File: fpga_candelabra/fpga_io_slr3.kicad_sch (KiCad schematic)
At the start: 1 part, among them U1 XCVU13P-B2104

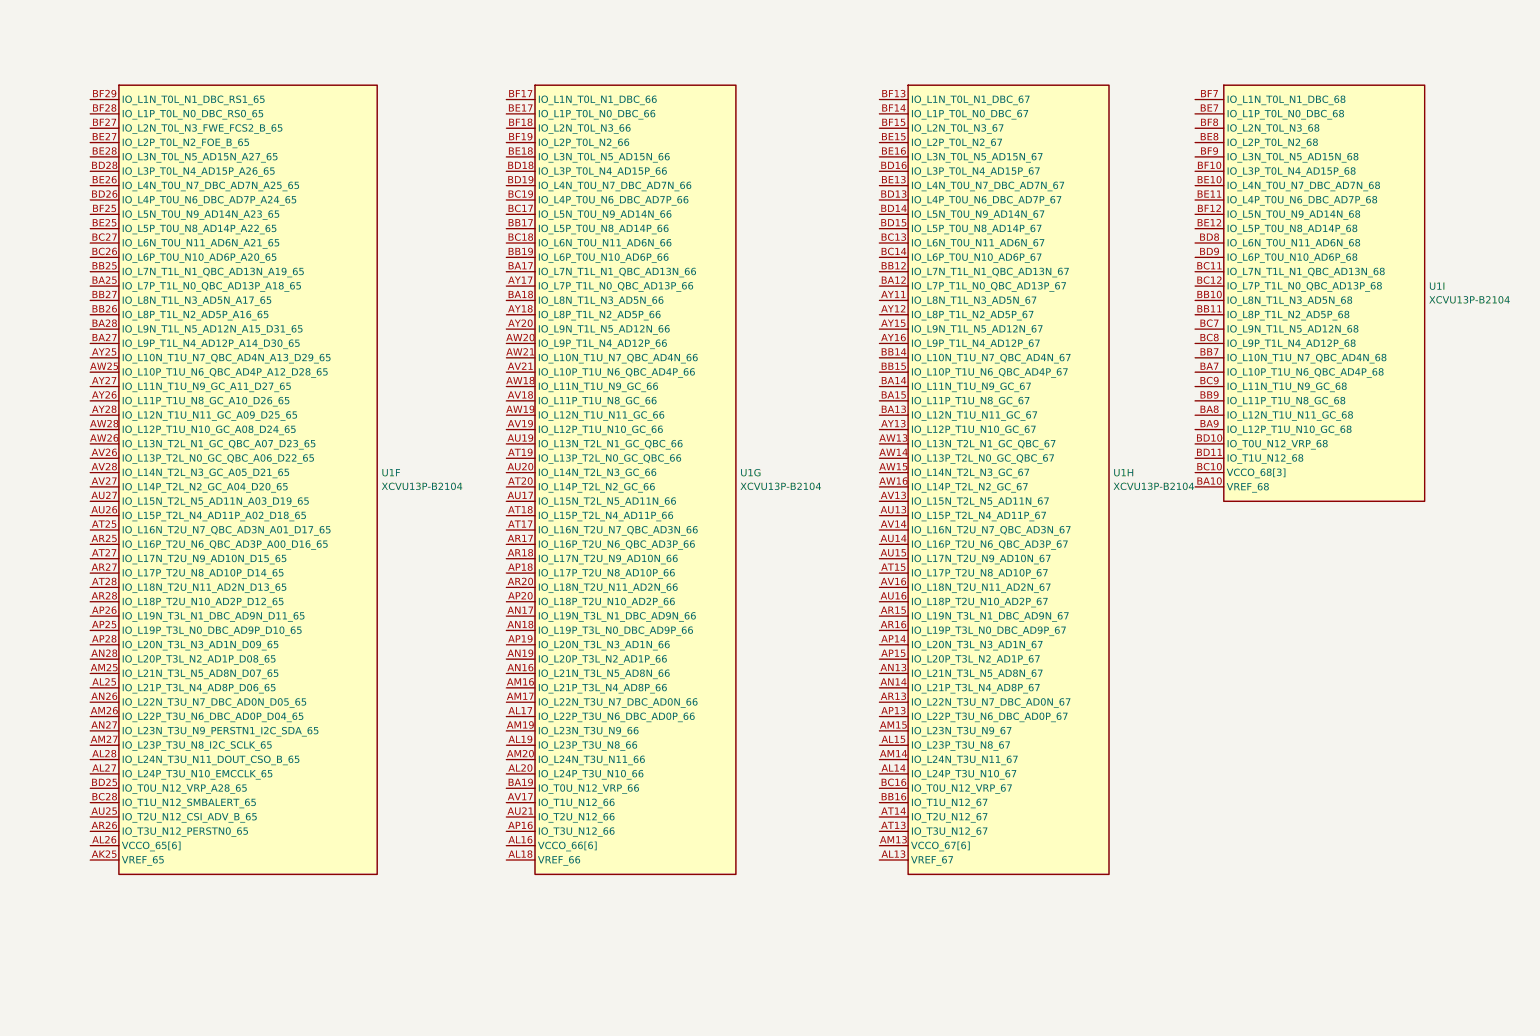
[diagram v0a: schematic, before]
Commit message: fpga_candelabra: reorganize fpga io and mgt by SLR
- Rename sch sheets
- Add prelimary DDR and PCIE Bank/Quad allocation

Signed-off-by: Yichuan Gao <gaoyichuan000@gmail.com>
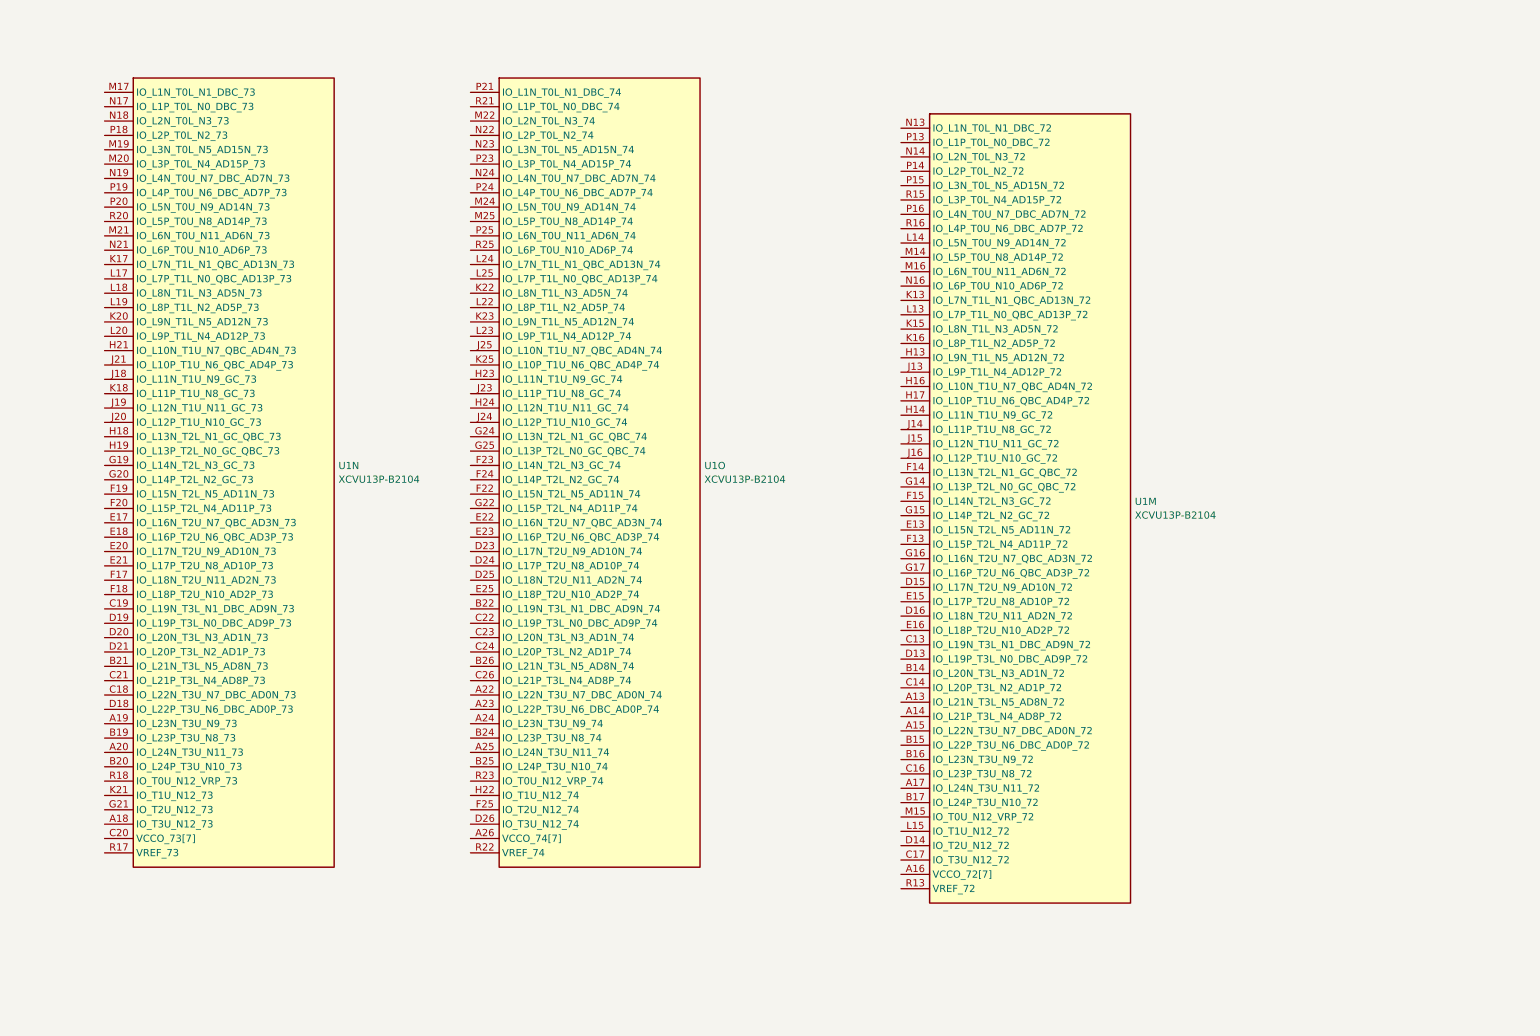
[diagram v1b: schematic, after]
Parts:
- removed U1: XCVU13P-B2104, CHIPSAlliance_Package_BGA:Xilinx_FHGB2104_VU13P_PkgLength, symbol CHIPSAlliance_FPGA_Xilinx_Virtex_UltraScale_Plus:XCVU13P-B2104
- added U1: XCVU13P-B2104, CHIPSAlliance_Package_BGA:Xilinx_FHGB2104_VU13P_PkgLength, symbol CHIPSAlliance_FPGA_Xilinx_Virtex_UltraScale_Plus:XCVU13P-B2104
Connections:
- new net: U1.A26 (VCCO_74[7]), U1.B23 (VCCO_74[7]), U1.E24 (VCCO_74[7]), U1.H25 (VCCO_74[7]), U1.J22 (VCCO_74[7]), U1.M23 (VCCO_74[7]), U1.R24 (VCCO_74[7])
- new net: U1.A16 (VCCO_72[7]), U1.B13 (VCCO_72[7]), U1.E14 (VCCO_72[7]), U1.H15 (VCCO_72[7]), U1.L16 (VCCO_72[7]), U1.M13 (VCCO_72[7]), U1.R14 (VCCO_72[7])
- new net: U1.C20 (VCCO_73[7]), U1.D17 (VCCO_73[7]), U1.F21 (VCCO_73[7]), U1.G18 (VCCO_73[7]), U1.K19 (VCCO_73[7]), U1.N20 (VCCO_73[7]), U1.P17 (VCCO_73[7])

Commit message: fpga_candelabra: use bus alias to connect ddr4
Signed-off-by: Yichuan Gao <gaoyichuan000@gmail.com>
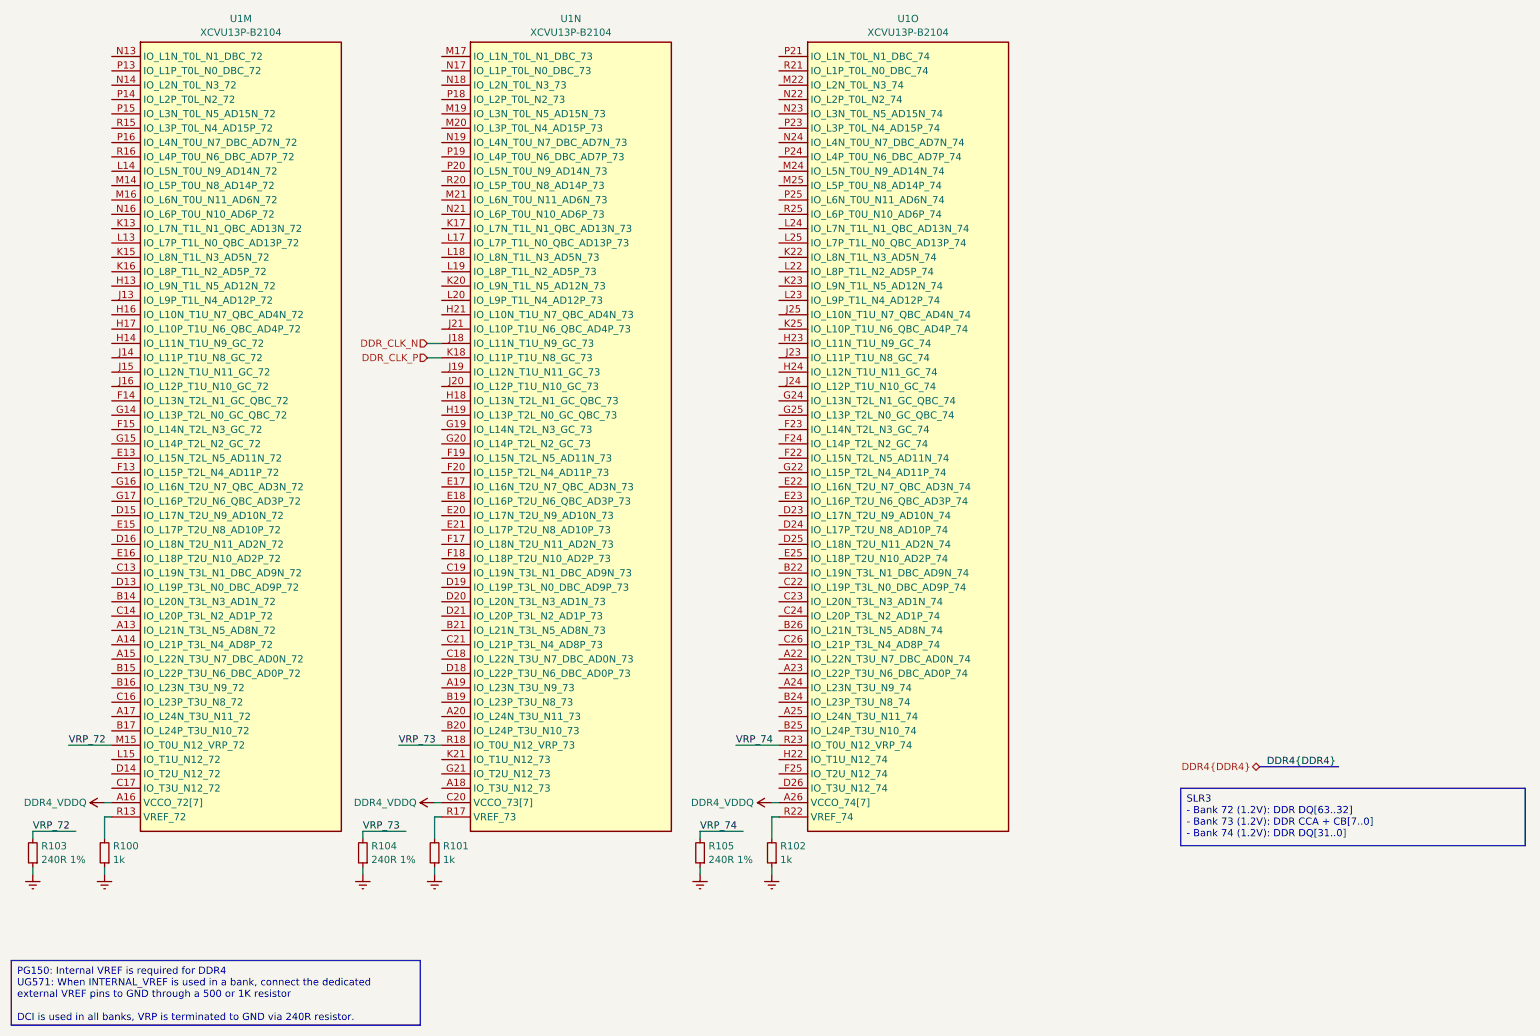
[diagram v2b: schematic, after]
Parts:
- added R100, R101, R102: 1k, Resistor_SMD:R_0402_1005Metric, symbol Device:R_Small
- added R103, R104, R105: 240R 1%, Resistor_SMD:R_0402_1005Metric, symbol Device:R_Small
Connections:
- net DDR4_VDDQ: now reaches U1.A26 (VCCO_74[7]), U1.B23 (VCCO_74[7]), U1.E24 (VCCO_74[7]), U1.H25 (VCCO_74[7]), U1.J22 (VCCO_74[7]), U1.M23 (VCCO_74[7]), U1.R24 (VCCO_74[7])
- net DDR4_VDDQ: now also U1.A16 (VCCO_72[7]), U1.B13 (VCCO_72[7]), U1.C20 (VCCO_73[7]), U1.D17 (VCCO_73[7]), U1.E14 (VCCO_72[7]), U1.F21 (VCCO_73[7]), U1.G18 (VCCO_73[7]), U1.H15 (VCCO_72[7]), U1.K19 (VCCO_73[7]), U1.L16 (VCCO_72[7]), U1.M13 (VCCO_72[7]), U1.N20 (VCCO_73[7]), U1.P17 (VCCO_73[7]), U1.R14 (VCCO_72[7])
- net at U1.R22 (VREF_74): now also R102.2
- net VRP_74: now reaches U1.R23 (IO_T0U_N12_VRP_74)
- net VRP_74: now also R105.2
- net VRP_72: now reaches U1.M15 (IO_T0U_N12_VRP_72)
- net VRP_72: now also R103.2
- net at U1.R13 (VREF_72): now also R100.2
- net DDR_CLK_N: now reaches U1.J18 (IO_L11N_T1U_N9_GC_73)
- net DDR_CLK_P: now reaches U1.K18 (IO_L11P_T1U_N8_GC_73)
- net at U1.R17 (VREF_73): now also R101.2
- net VRP_73: now reaches U1.R18 (IO_T0U_N12_VRP_73)
- net VRP_73: now also R104.2
- new net Earth: R100.1, R101.1, R102.1, R103.1, R104.1, R105.1
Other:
- moved on the sheet: U1M, U1N, U1O

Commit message: fpga_candelabra: fix minor issues in ddr sch
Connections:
- net DDR_CLK_N renamed DDR_CLK-
- net DDR_CLK_P renamed DDR_CLK+
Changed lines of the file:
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@@
 		)
 	)
-	(hierarchical_label "DDR_CLK_P"
+	(hierarchical_label "DDR_CLK+"
 		(shape input)
 		(at 88.9 77.47 180)
@@
 		)
 	)
-	(hierarchical_label "DDR_CLK_N"
+	(hierarchical_label "DDR_CLK-"
 		(shape input)
 		(at 88.9 74.93 180)

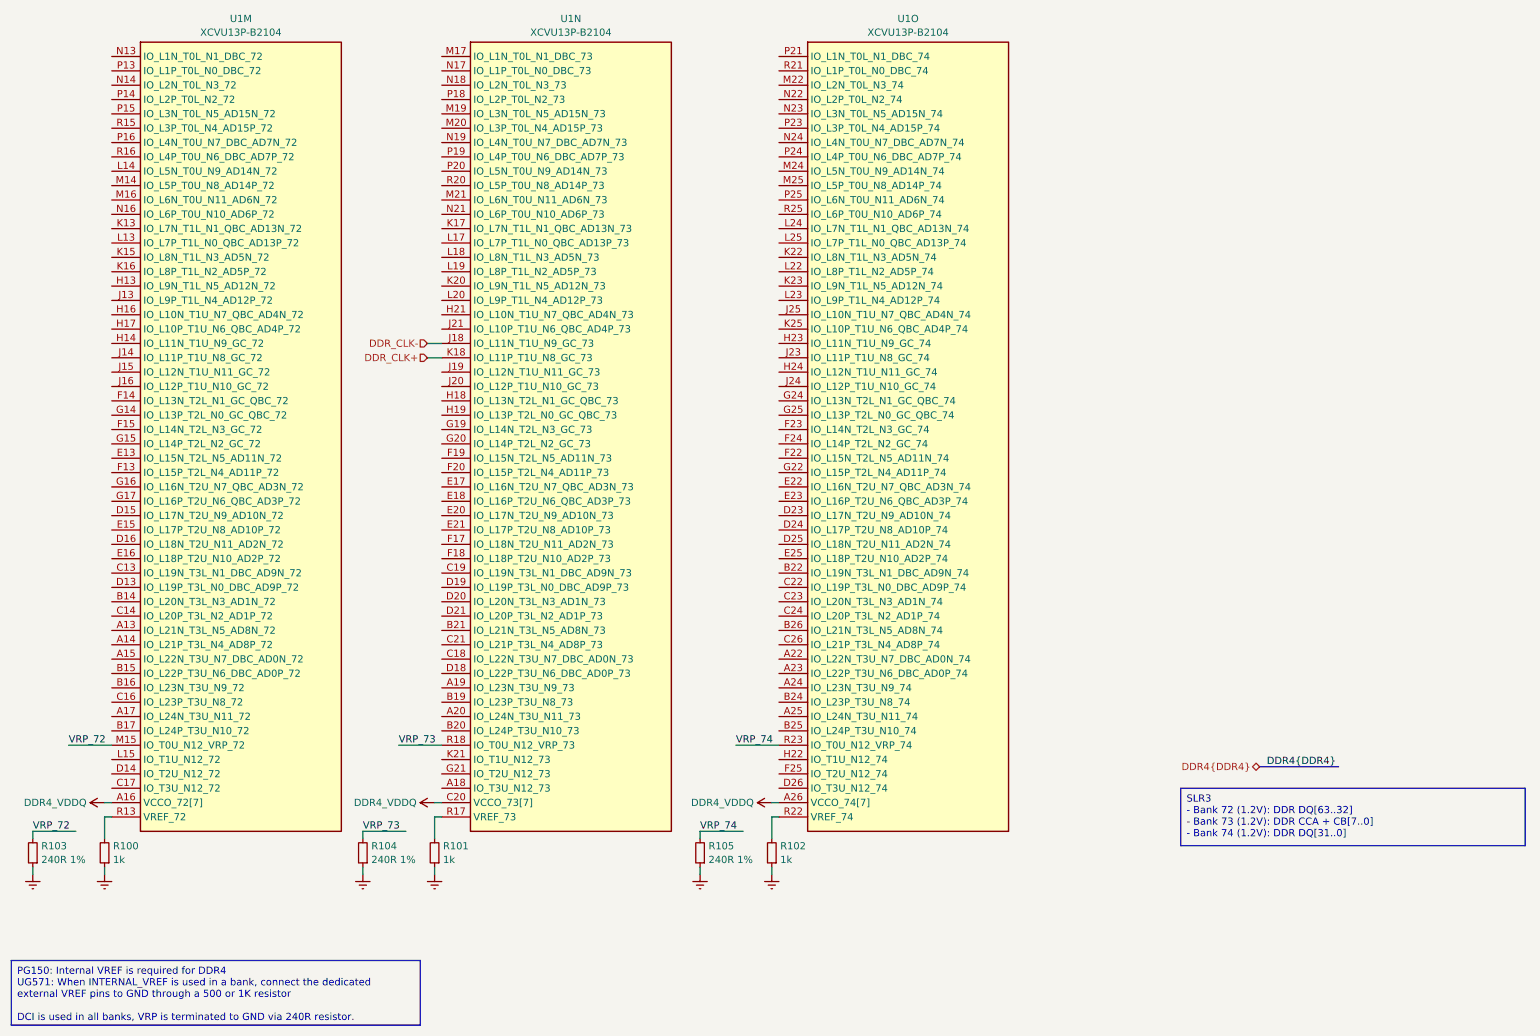
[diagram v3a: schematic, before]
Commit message: candelabra: add i-pex extension ports, remove FMC1
* update bank/mgt allocation
* add basic pcb floorplanning

Signed-off-by: Yichuan Gao <gaoyichuan000@gmail.com>
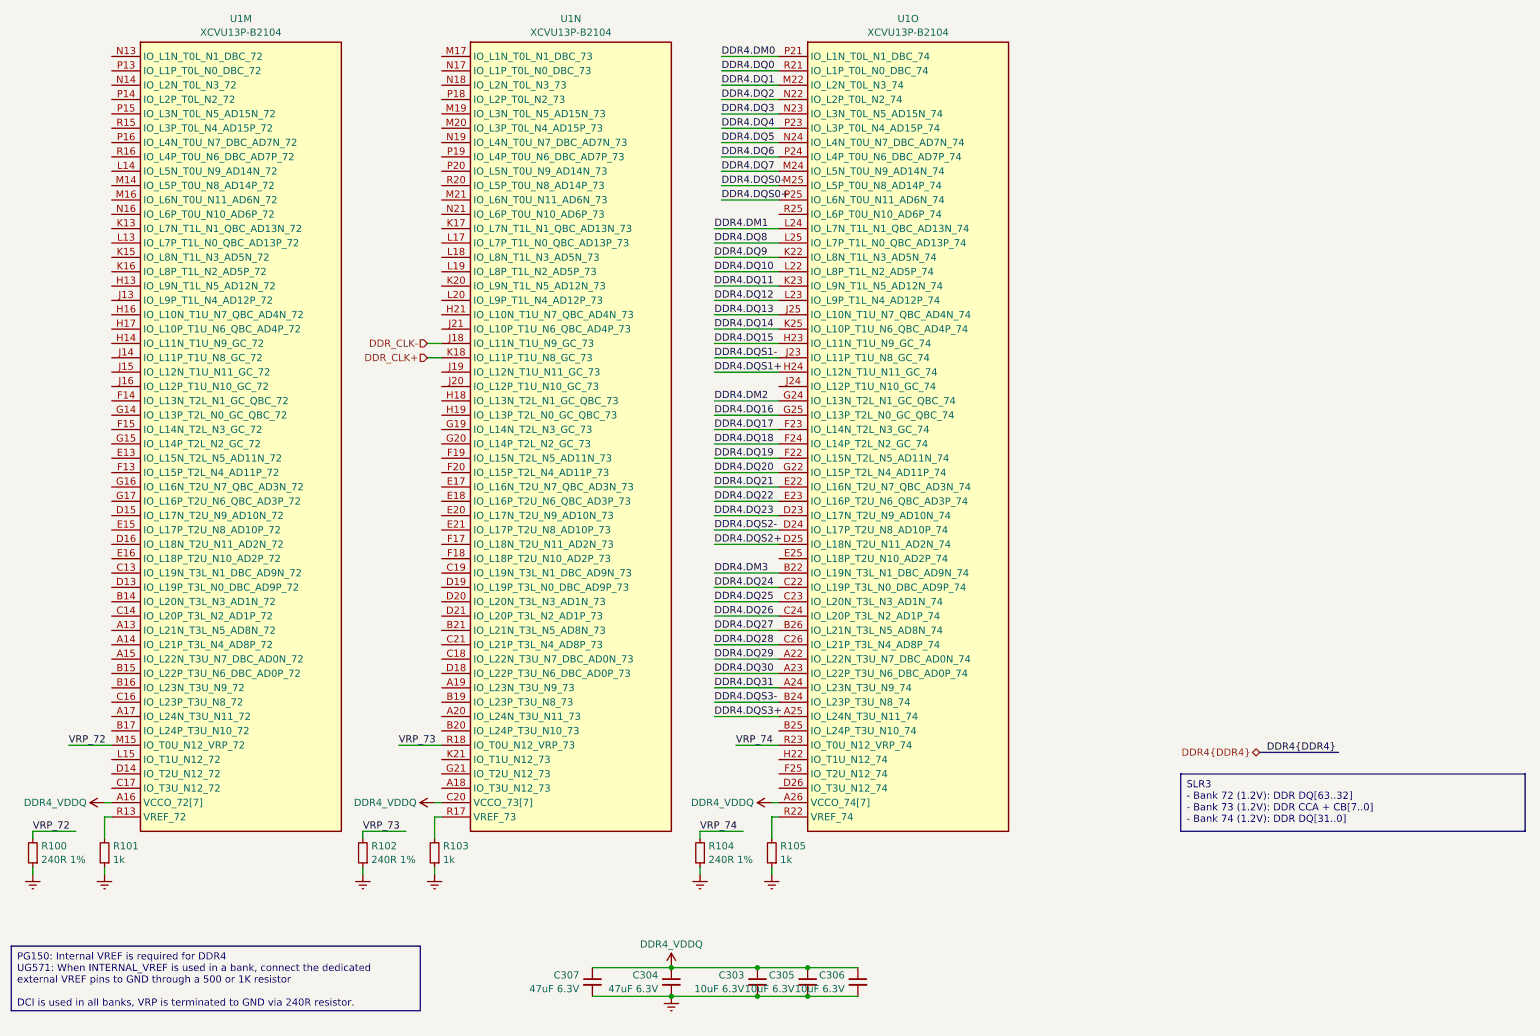
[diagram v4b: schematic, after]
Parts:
- added C303, C305, C306: 10uF 6.3V, Capacitor_SMD:C_0402_1005Metric, symbol Device:C_Small
- added C304, C307: 47uF 6.3V, Capacitor_SMD:C_0603_1608Metric, symbol Device:C_Small
- R100, R102: value 1k -> 240R 1%
- R103, R105: value 240R 1% -> 1k
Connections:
- net DDR4_VDDQ: now also C303.1, C304.1, C305.1, C306.1, C307.1
- net Earth: now also C303.2, C304.2, C305.2, C306.2, C307.2
- net VRP_72: now also R100.2; no longer R103.2
- net VRP_73: now also R102.2; no longer R104.2
- net VRP_74: now also R104.2; no longer R105.2
- net DDR4.DQ29: now reaches U1.A22 (IO_L22N_T3U_N7_DBC_AD0N_74)
- net DDR4.DQ30: now reaches U1.A23 (IO_L22P_T3U_N6_DBC_AD0P_74)
- net DDR4.DQ31: now reaches U1.A24 (IO_L23N_T3U_N9_74)
- net DDR4.DQS3+: now reaches U1.A25 (IO_L24N_T3U_N11_74)
- net DDR4.DM3: now reaches U1.B22 (IO_L19N_T3L_N1_DBC_AD9N_74)
- net DDR4.DQS3-: now reaches U1.B24 (IO_L23P_T3U_N8_74)
- net DDR4.DQ27: now reaches U1.B26 (IO_L21N_T3L_N5_AD8N_74)
- net DDR4.DQ24: now reaches U1.C22 (IO_L19P_T3L_N0_DBC_AD9P_74)
- net DDR4.DQ25: now reaches U1.C23 (IO_L20N_T3L_N3_AD1N_74)
- net DDR4.DQ26: now reaches U1.C24 (IO_L20P_T3L_N2_AD1P_74)
- net DDR4.DQ28: now reaches U1.C26 (IO_L21P_T3L_N4_AD8P_74)
- net DDR4.DQ23: now reaches U1.D23 (IO_L17N_T2U_N9_AD10N_74)
- net DDR4.DQS2-: now reaches U1.D24 (IO_L17P_T2U_N8_AD10P_74)
- net DDR4.DQS2+: now reaches U1.D25 (IO_L18N_T2U_N11_AD2N_74)
- net DDR4.DQ21: now reaches U1.E22 (IO_L16N_T2U_N7_QBC_AD3N_74)
- net DDR4.DQ22: now reaches U1.E23 (IO_L16P_T2U_N6_QBC_AD3P_74)
- net DDR4.DQ19: now reaches U1.F22 (IO_L15N_T2L_N5_AD11N_74)
- net DDR4.DQ17: now reaches U1.F23 (IO_L14N_T2L_N3_GC_74)
- net DDR4.DQ18: now reaches U1.F24 (IO_L14P_T2L_N2_GC_74)
- net DDR4.DQ20: now reaches U1.G22 (IO_L15P_T2L_N4_AD11P_74)
- net DDR4.DM2: now reaches U1.G24 (IO_L13N_T2L_N1_GC_QBC_74)
- net DDR4.DQ16: now reaches U1.G25 (IO_L13P_T2L_N0_GC_QBC_74)
- net DDR4.DQ15: now reaches U1.H23 (IO_L11N_T1U_N9_GC_74)
- net DDR4.DQS1+: now reaches U1.H24 (IO_L12N_T1U_N11_GC_74)
- net DDR4.DQS1-: now reaches U1.J23 (IO_L11P_T1U_N8_GC_74)
- net DDR4.DQ13: now reaches U1.J25 (IO_L10N_T1U_N7_QBC_AD4N_74)
- net DDR4.DQ9: now reaches U1.K22 (IO_L8N_T1L_N3_AD5N_74)
- net DDR4.DQ11: now reaches U1.K23 (IO_L9N_T1L_N5_AD12N_74)
- net DDR4.DQ14: now reaches U1.K25 (IO_L10P_T1U_N6_QBC_AD4P_74)
- net DDR4.DQ10: now reaches U1.L22 (IO_L8P_T1L_N2_AD5P_74)
- net DDR4.DQ12: now reaches U1.L23 (IO_L9P_T1L_N4_AD12P_74)
- net DDR4.DM1: now reaches U1.L24 (IO_L7N_T1L_N1_QBC_AD13N_74)
- net DDR4.DQ8: now reaches U1.L25 (IO_L7P_T1L_N0_QBC_AD13P_74)
- net DDR4.DQ1: now reaches U1.M22 (IO_L2N_T0L_N3_74)
- net DDR4.DQ7: now reaches U1.M24 (IO_L5N_T0U_N9_AD14N_74)
- net DDR4.DQS0-: now reaches U1.M25 (IO_L5P_T0U_N8_AD14P_74)
- net DDR4.DQ2: now reaches U1.N22 (IO_L2P_T0L_N2_74)
- net DDR4.DQ3: now reaches U1.N23 (IO_L3N_T0L_N5_AD15N_74)
- net DDR4.DQ5: now reaches U1.N24 (IO_L4N_T0U_N7_DBC_AD7N_74)
- net DDR4.DM0: now reaches U1.P21 (IO_L1N_T0L_N1_DBC_74)
- net DDR4.DQ4: now reaches U1.P23 (IO_L3P_T0L_N4_AD15P_74)
- net DDR4.DQ6: now reaches U1.P24 (IO_L4P_T0U_N6_DBC_AD7P_74)
- net DDR4.DQS0+: now reaches U1.P25 (IO_L6N_T0U_N11_AD6N_74)
- net DDR4.DQ0: now reaches U1.R21 (IO_L1P_T0L_N0_DBC_74)
- net at U1.R22 (VREF_74): now also R105.2; no longer R102.2
- net at U1.R13 (VREF_72): now also R101.2; no longer R100.2
- net at U1.R17 (VREF_73): now also R103.2; no longer R101.2
